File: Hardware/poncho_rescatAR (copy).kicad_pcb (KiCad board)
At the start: 2 copper layers, 34 parts, among them P1 5V_OUT, P2 CONN_8, SW1 Reset_ciaa, U1 LM317T, U2 LM7805

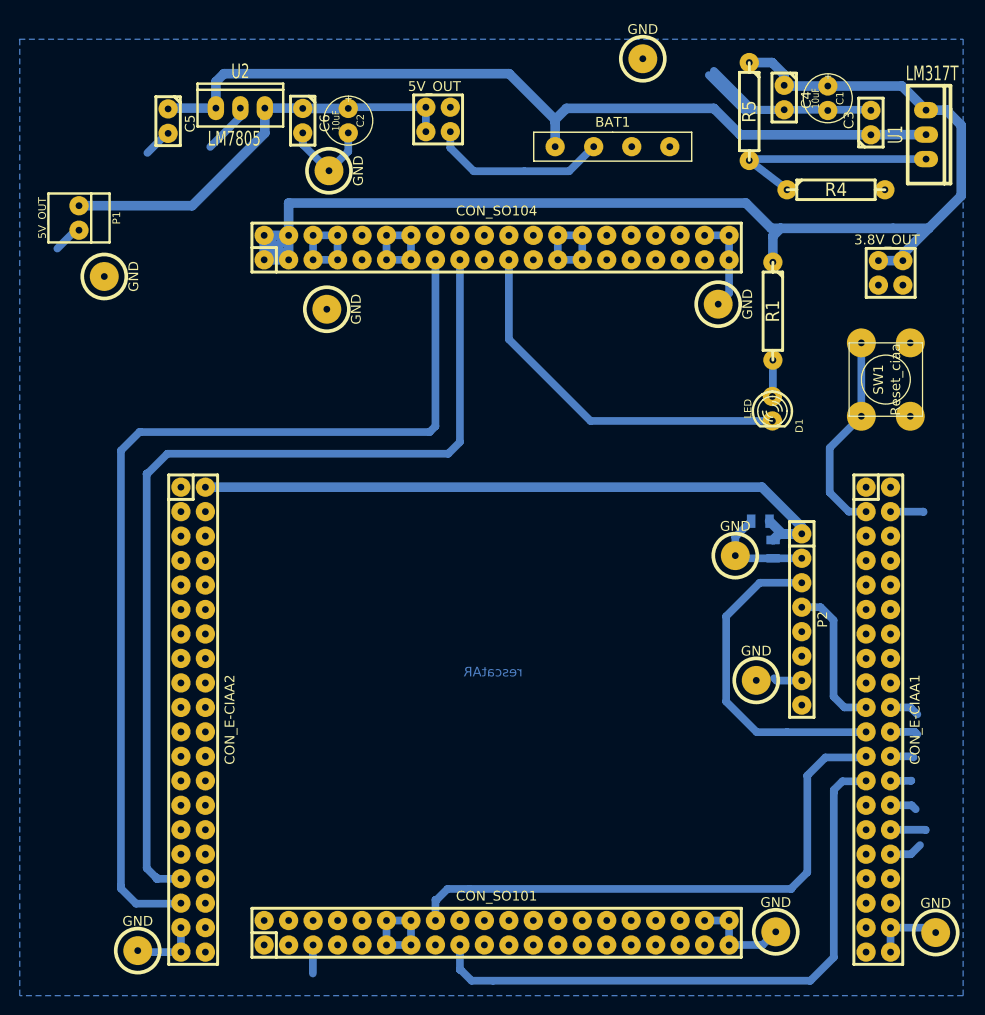
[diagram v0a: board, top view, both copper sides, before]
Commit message: Agregado de capacitores en la alimentacion del acelerometro y pulsador de reset de la ciaa
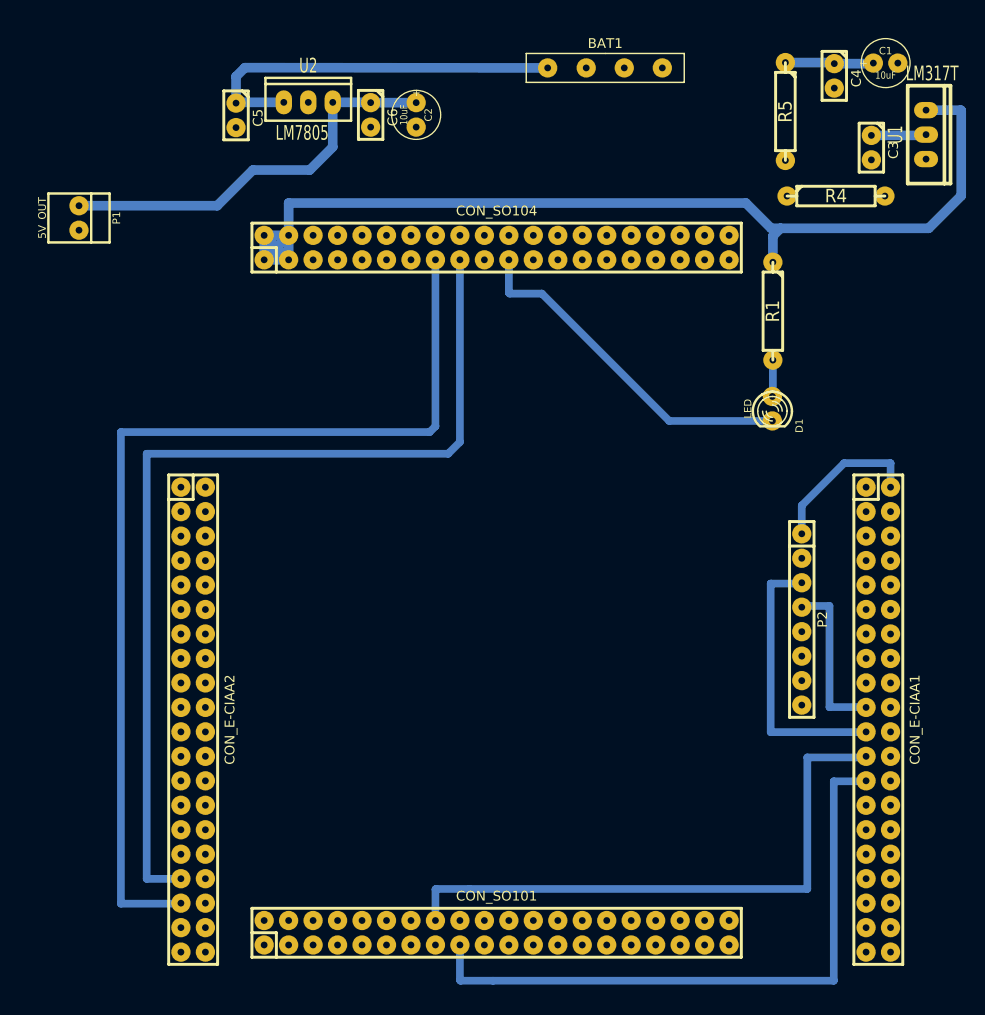
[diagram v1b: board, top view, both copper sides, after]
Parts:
- removed 3.8V_OUT, 5V_OUT: Val**, PIN_ARRAY_2X2
- removed C7: 0.1uF, SM0805
- removed C8: 10uF, SM0805
- removed GND (x10): P***, 1pin
- removed SW1: Reset_ciaa, SW_PUSH_SMALL
- C3, C4, C5, C6: value 0.1uF -> 0.1
- moved BAT1 8.21 mm to (226.0, 28.7)
- moved C2 7.08 mm to (206.4, 33.5)
- moved C5 7.08 mm to (187.7, 33.6)
- moved C6 7.08 mm to (201.7, 33.5)
- moved U2 7.08 mm to (195.2, 32.2)
- moved C1 7.02 mm to (255.1, 28.2), turned to 0 degrees
- moved C4 5.67 mm to (249.8, 29.5)
- moved R5 3.75 mm to (244.7, 33.2)
- moved C3 2.60 mm to (253.6, 37.0), turned to 270 degrees
- moved R4 0.65 mm to (249.9, 42.0)
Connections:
- CON_E-CIAA1 pad 3: /RESET -> (no net)
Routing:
- net /GND: track 184.1 -> 0.00 mm
- net /VCC_5V: track 71.5 -> 16.5 mm
- net VCC: track 88.2 -> 46.2 mm
- net N-000002: track 23.4 -> 0.00 mm
- net /RESET: track 21.5 -> 0.00 mm
- net /VCC_3.8V: track 136.6 -> 118.6 mm
- net /I2C_SCL: track 34.0 -> 28.6 mm
- net /STATUS_LED: track 39.1 -> 36.3 mm
- net /RS232_RXD: track 58.9 -> 61.6 mm
- net /RS232_TXD: track 64.0 -> 66.6 mm
- net N-000003: track 44.3 -> 42.2 mm
- net /GE864_ON_OFF: track 103.4 -> 105.4 mm
- net /I2C_SDA: track 15.6 -> 17.2 mm
- net /GE864_RESET: track 98.4 -> 99.6 mm
- removed copper zone on B.Cu, net /GND
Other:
- board text removed: "rescatAR"
